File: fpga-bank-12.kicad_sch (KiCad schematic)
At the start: 5 parts, among them U1 XC7K410T-2FFG900I

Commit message: Bump revision to 1.0.0. Update name on schematic and PCB sheets
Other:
- title: K410T devboard -> Kintex 410T devboard

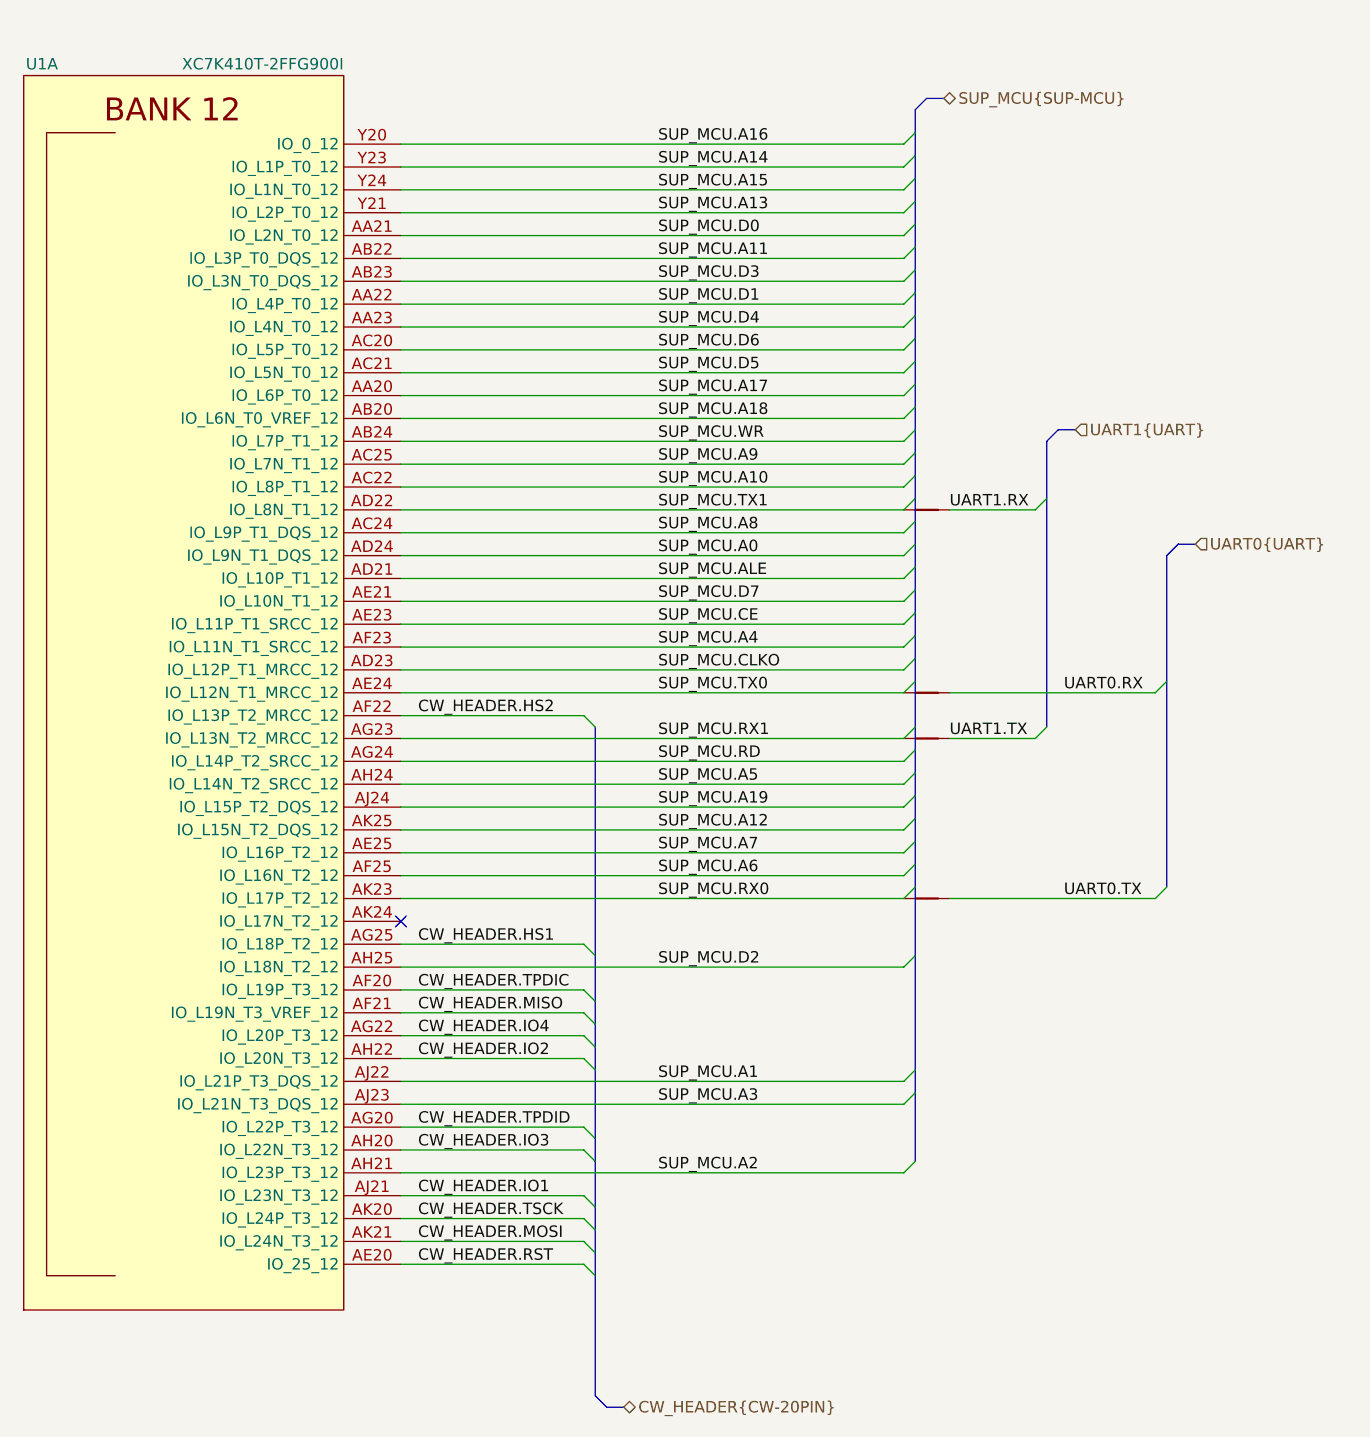
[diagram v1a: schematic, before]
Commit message: Introduce component standardization
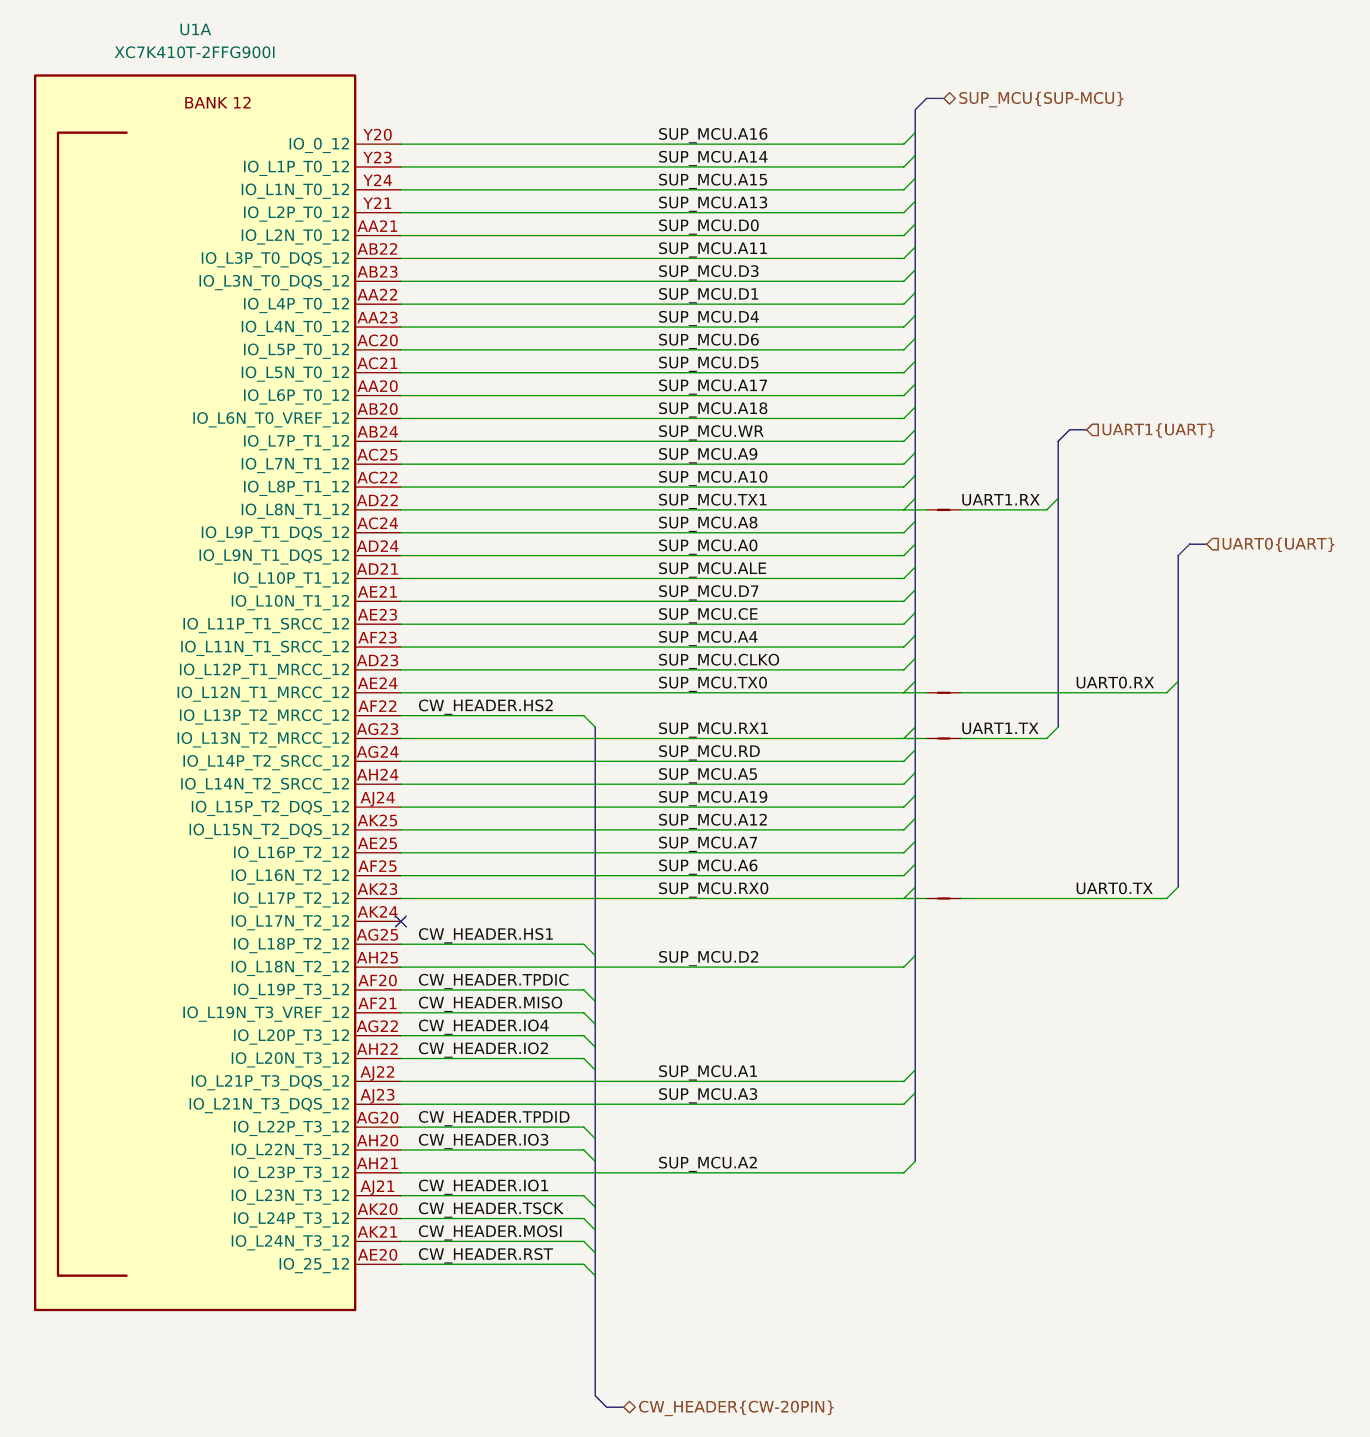
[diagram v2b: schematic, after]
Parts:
- NT15, NT16, NT17, NT18: value NetTie_2 -> Net-Tie_2; symbol K410T-devboard:NetTie_2 -> K410T-devboard:Net-Tie_2; Author (none) -> Antmicro; License (none) -> Apache-2.0
- U1: Author (none) -> Antmicro; License (none) -> Apache-2.0

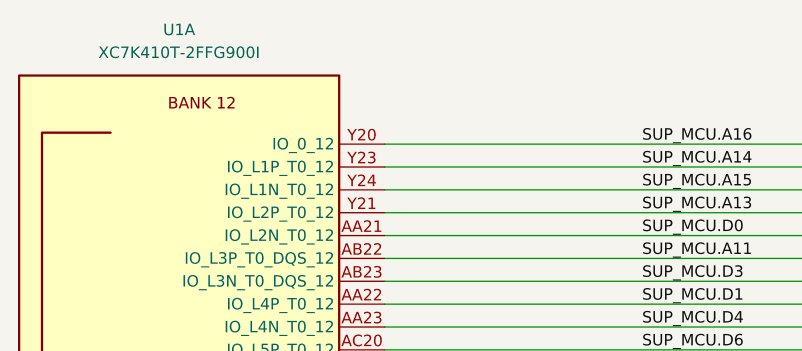
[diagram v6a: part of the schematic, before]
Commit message: [#55729] Change Manufacturer to AMD-Xilinx
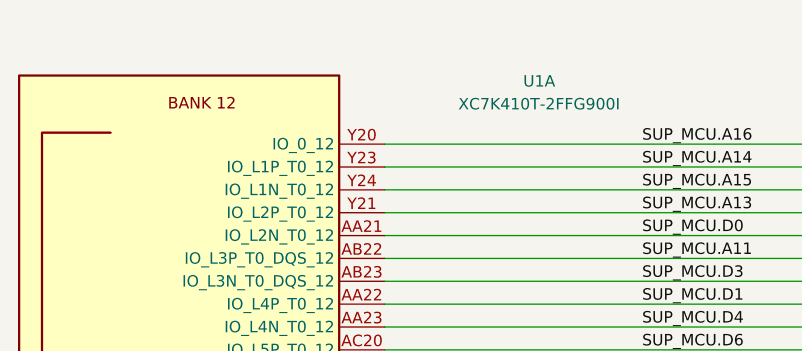
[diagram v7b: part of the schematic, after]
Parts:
- U1: Manufacturer Xilinx -> AMD-Xilinx
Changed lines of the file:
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@@
   (symbol (lib_id "K410T-devboard:XC7K410T-2FFG900I") (at 143.51 83.82 0) (unit 1)
     (in_bom yes) (on_board yes) (dnp no) (fields_autoplaced)
-    (property "Reference" "U1" (at 120.65 71.12 0)
+    (property "Reference" "U1" (at 160.655 76.835 0)
       (effects (font (size 1.27 1.27) (thickness 0.15)))
     )
-    (property "Value" "XC7K410T-2FFG900I" (at 120.65 73.66 0)
+    (property "Value" "XC7K410T-2FFG900I" (at 160.655 79.375 0)
       (effects (font (size 1.27 1.27) (thickness 0.15)))
     )
@@
       (effects (font (size 1.27 1.27) (thickness 0.15)) (justify left bottom) hide)
     )
-    (property "Manufacturer" "Xilinx" (at 143.51 62.23 0)
+    (property "Manufacturer" "AMD-Xilinx" (at 143.51 62.23 0)
       (effects (font (size 1.27 1.27) (thickness 0.15)) (justify left bottom) hide)
     )
@@
           (reference "U1") (unit 1)
         )
+        (path "/c1489e7c-896d-4046-acd4-3929998e87dc/020031b8-7f27-4e26-b74c-26be7f0881a9"
+          (reference "U1") (unit 1)
+        )
